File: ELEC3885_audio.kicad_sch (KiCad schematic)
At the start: 43 parts, among them J1 MicInstIn, J2 LineIn, J3 HeadPhoneOut, J4 Conn_01x05_Female, J5 LineOutR, J6 LineOutL, U1 NE5532, U2 AP7313, U3 SGTL5000XNLA3

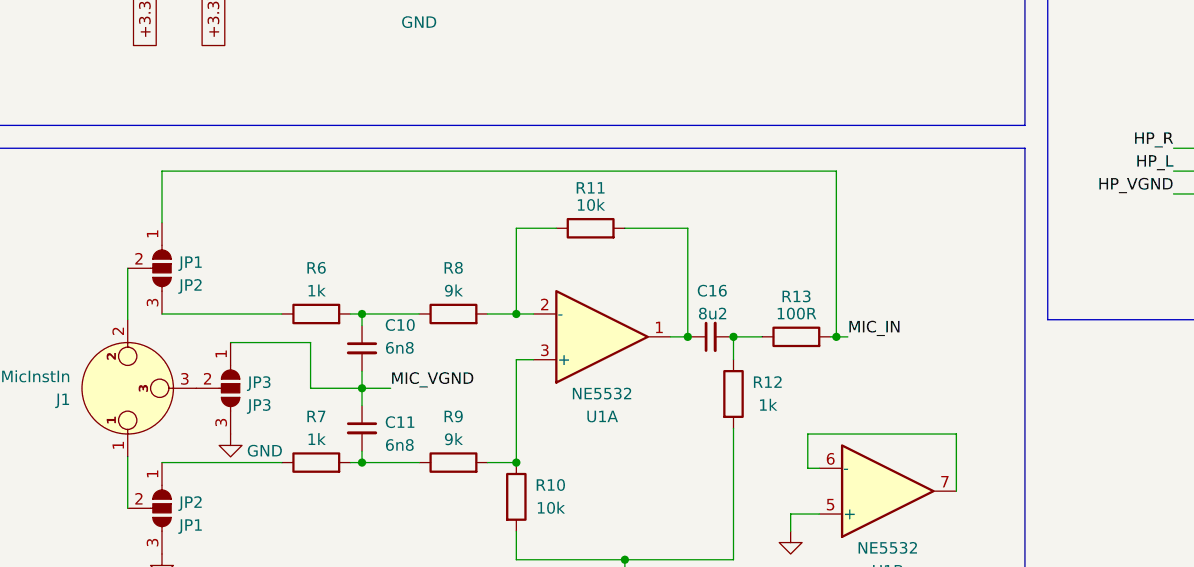
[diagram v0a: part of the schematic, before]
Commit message: Testpoints added, silkscreen cleaned
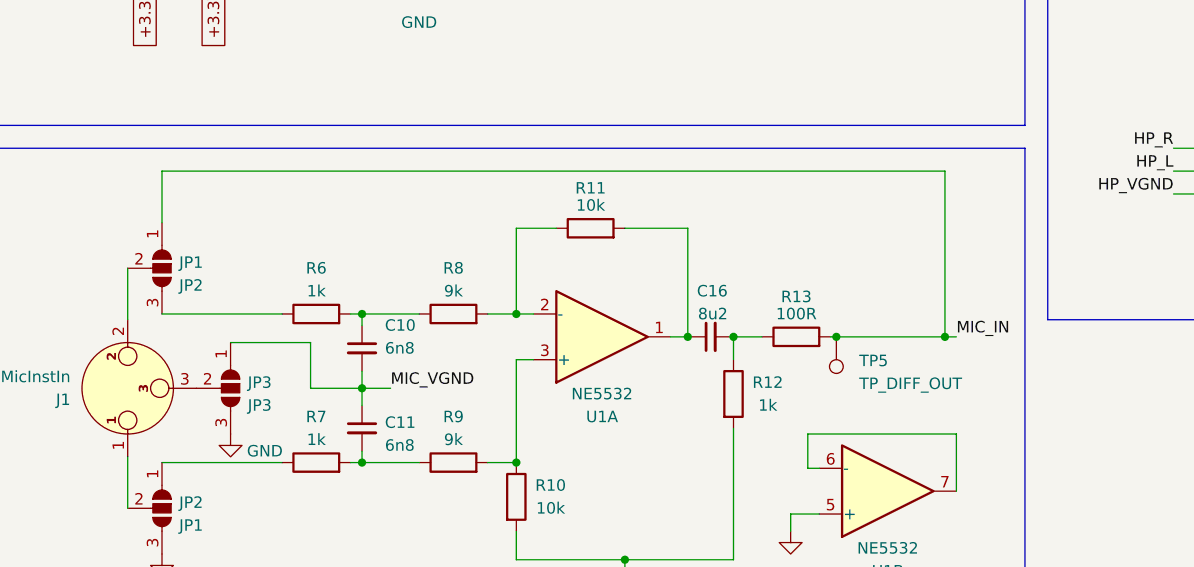
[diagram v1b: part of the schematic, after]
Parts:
- added TP5: TP_DIFF_OUT, TestPoint:TestPoint_Pad_D1.0mm, symbol Connector:TestPoint
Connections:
- net MIC_IN: now also TP5.1

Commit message: Footprints updated except codec
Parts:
- C16: footprint Capacitor_SMD:C_0402_1005Metric -> Capacitor_SMD:C_0603_1608Metric
- R8, R9: footprint Resistor_SMD:R_0603_1608Metric -> Resistor_SMD:R_0805_2012Metric
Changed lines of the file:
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@@
       (effects (font (size 1.27 1.27)))
     )
-    (property "Footprint" "Resistor_SMD:R_0603_1608Metric" (at 110.49 181.483 90)
+    (property "Footprint" "Resistor_SMD:R_0805_2012Metric" (at 110.49 181.483 90)
       (effects (font (size 1.27 1.27)) hide)
     )
@@
       (effects (font (size 1.27 1.27)) (justify left))
     )
-    (property "Footprint" "Capacitor_SMD:C_0402_1005Metric" (at 139.065 165.735 0)
+    (property "Footprint" "Capacitor_SMD:C_0603_1608Metric" (at 139.065 165.735 0)
       (effects (font (size 1.27 1.27)) hide)
     )
@@
       (effects (font (size 1.27 1.27)))
     )
-    (property "Footprint" "Resistor_SMD:R_0603_1608Metric" (at 110.49 164.973 90)
-      (effects (font (size 1.27 1.27)) hide)
-    )
+    (property "Footprint" "Resistor_SMD:R_0805_2012Metric" (at 110.49 164.973 90)
+      (effects (font (size 1.27 1.27)) hide)
+    )

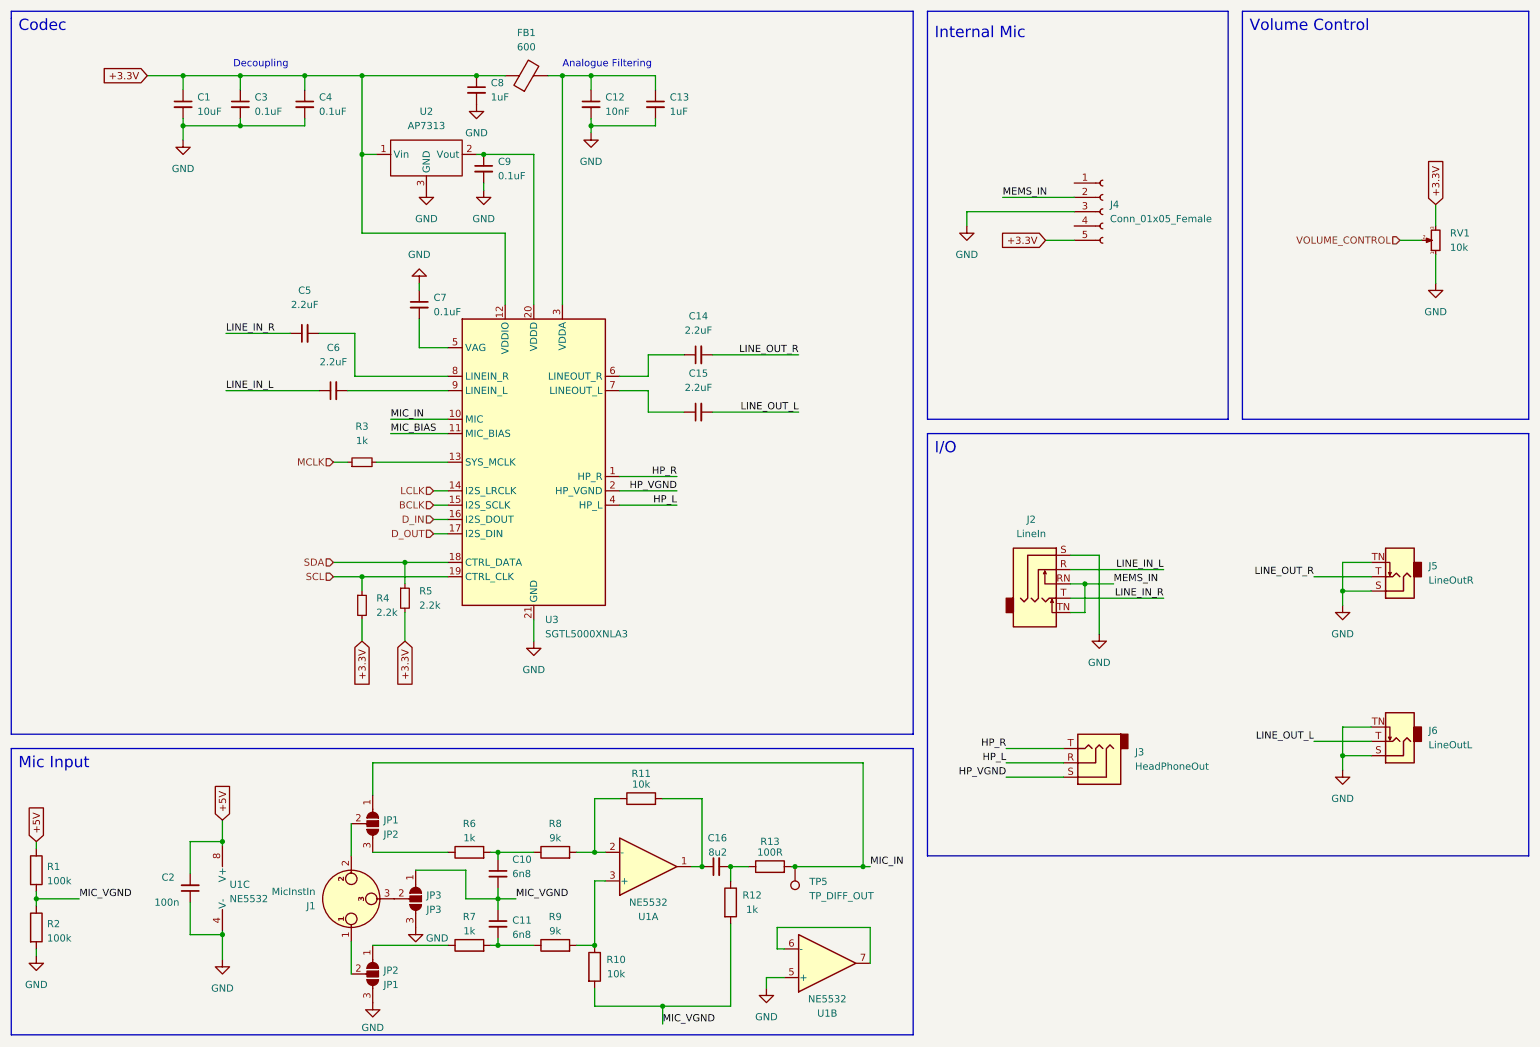
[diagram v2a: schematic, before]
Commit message: SGTL5000 package switched to QFN32
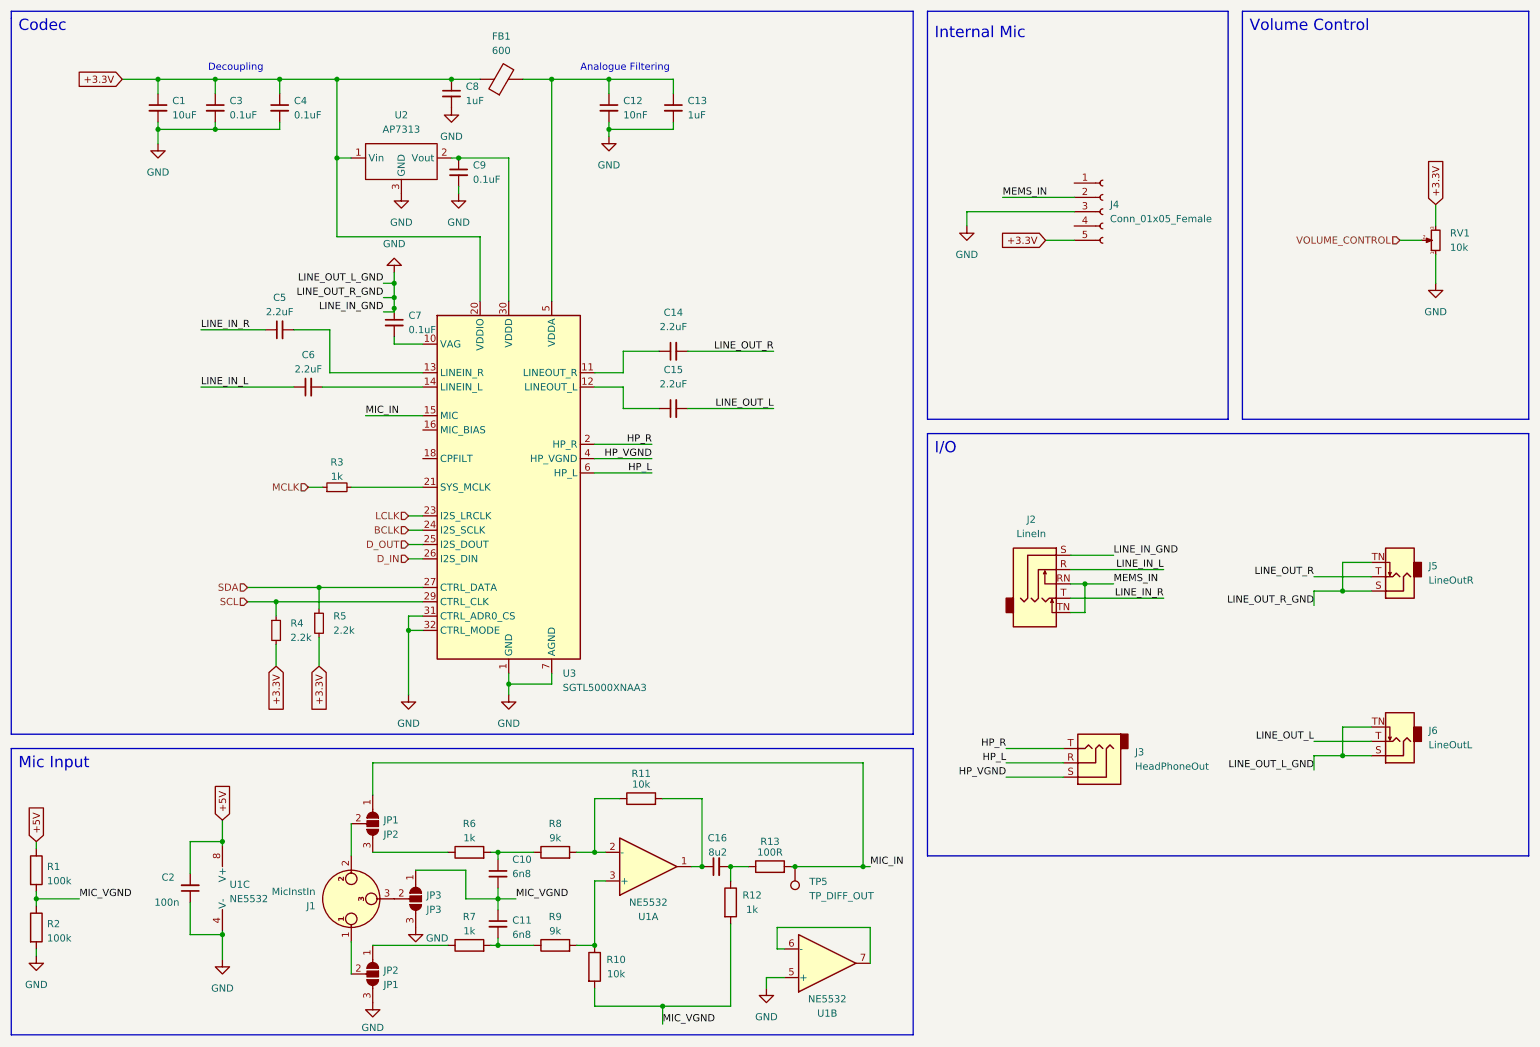
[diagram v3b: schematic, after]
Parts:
- removed U3: SGTL5000XNLA3, Package_DFN_QFN:QFN-20-1EP_3x3mm_P0.4mm_EP1.65x1.65mm, symbol Audio:SGTL5000XNLA3
- added U3: SGTL5000XNAA3, Package_DFN_QFN:QFN-32-1EP_5x5mm_P0.5mm_EP3.6x3.6mm, symbol Audio:SGTL5000XNAA3
- U2: footprint LukeLibrary:SOT23 -> Luke_library:SOT23
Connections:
- net +3.3V: now also U3.20 (VDDIO)
- net BCLK: now also U3.24 (I2S_SCLK)
- net D_IN: now also U3.26 (I2S_DIN)
- net D_OUT: now also U3.25 (I2S_DOUT)
- net GND: now also U3.1 (GND), U3.3 (GND), U3.31 (CTRL_ADR0_CS), U3.32 (CTRL_MODE), U3.33 (GND), U3.7 (AGND)
- net HP_L: now also U3.6 (HP_L)
- net HP_R: now also U3.2 (HP_R)
- net HP_VGND: now also U3.4 (HP_VGND)
- net LCLK: now also U3.23 (I2S_LRCLK)
- net MIC_IN: now also U3.15 (MIC)
- net SCL: now also U3.29 (CTRL_CLK)
- net SDA: now also U3.27 (CTRL_DATA)
- net at C12.1, C13.1, FB1.2: now also U3.5 (VDDA)
- net at C6.2: now also U3.14 (LINEIN_L)
- net at R3.2: now also U3.21 (SYS_MCLK)
- net at C15.1: now also U3.12 (LINEOUT_L)
- net at C9.1, U2.2 (Vout): now also U3.30 (VDDD)
- net at C7.2: now also U3.10 (VAG)
- net at C14.1: now also U3.11 (LINEOUT_R)
- net at C5.2: now also U3.13 (LINEIN_R)
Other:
- moved on the sheet: C1, C12, C13, C14, C15, C3, C4, C5, C6, C7, C8, C9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

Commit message: Rev4 ordered
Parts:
- J3: footprint Connector_Audio:Jack_3.5mm_CUI_SJ-3523-SMT_Horizontal -> Connector_Audio:Jack_3.5mm_CUI_SJ1-3533NG_Horizontal
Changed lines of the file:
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@@
   (junction (at 117.475 179.705) (diameter 0) (color 0 0 0 0)
   )
-  (junction (at 165.1 165.735) (diameter 0) (color 0 0 0 0)
-  )
   (junction (at 100.33 179.705) (diameter 0) (color 0 0 0 0)
   )
@@
   (junction (at 50.165 26.035) (diameter 0) (color 0 0 0 0)
   )
+  (junction (at 156.21 165.735) (diameter 0) (color 0 0 0 0)
+  )
   (junction (at 40.005 26.035) (diameter 0) (color 0 0 0 0)
   )
@@
     (stroke (width 0) (type default))
   )
-  (wire (pts (xy 153.035 165.735) (xy 165.1 165.735))
+  (wire (pts (xy 153.035 165.735) (xy 156.21 165.735))
     (stroke (width 0) (type default))
   )
@@
     (stroke (width 0) (type default))
   )
+  (wire (pts (xy 156.21 165.735) (xy 166.37 165.735))
+    (stroke (width 0) (type default))
+  )
   (wire (pts (xy 149.86 180.34) (xy 149.86 176.53))
     (stroke (width 0) (type default))
@@
     (stroke (width 0) (type default))
   )
-  (wire (pts (xy 165.1 165.735) (xy 166.37 165.735))
-    (stroke (width 0) (type default))
-  )
   (wire (pts (xy 100.33 179.705) (xy 106.68 179.705))
     (stroke (width 0) (type default))
@@
     (stroke (width 0) (type default))
   )
-  (wire (pts (xy 165.1 147.32) (xy 165.1 165.735))
+  (wire (pts (xy 156.21 147.32) (xy 156.21 165.735))
     (stroke (width 0) (type default))
   )
@@
     (stroke (width 0) (type default))
   )
-  (wire (pts (xy 78.105 147.32) (xy 165.1 147.32))
+  (wire (pts (xy 78.105 147.32) (xy 156.21 147.32))
     (stroke (width 0) (type default))
   )
@@
       (effects (font (size 1.27 1.27)) (justify right))
     )
-    (property "Footprint" "Connector_Audio:Jack_3.5mm_CUI_SJ-3523-SMT_Horizontal" (at 205.74 147.32 0)
-      (effects (font (size 1.27 1.27)) hide)
-    )
+    (property "Footprint" "Connector_Audio:Jack_3.5mm_CUI_SJ1-3533NG_Horizontal" (at 205.74 147.32 0)
+      (effects (font (size 1.27 1.27)) hide)
+    )
